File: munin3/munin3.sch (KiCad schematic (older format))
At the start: 79 parts, among them J1 Conn_Coaxial, J2 Conn_Coaxial, J3 Conn_01x02_Male, J4 Conn_01x02_Male, T1 Q_NMOS_DSG, T2 Q_NMOS_DSG, T3 BSS84, T4 BST82, U1 MC78L08_SO8, U2 LMC6482

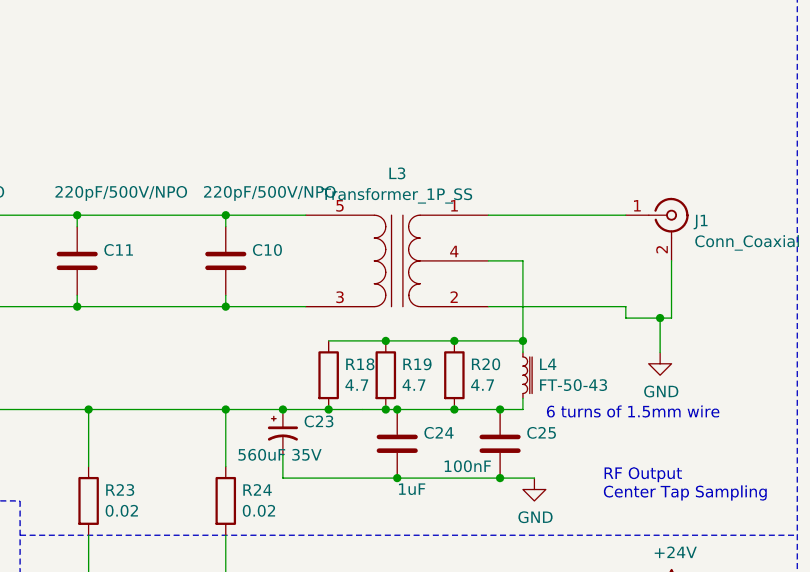
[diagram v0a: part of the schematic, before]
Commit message: Fixed drain connection, fixed final xfmr connection
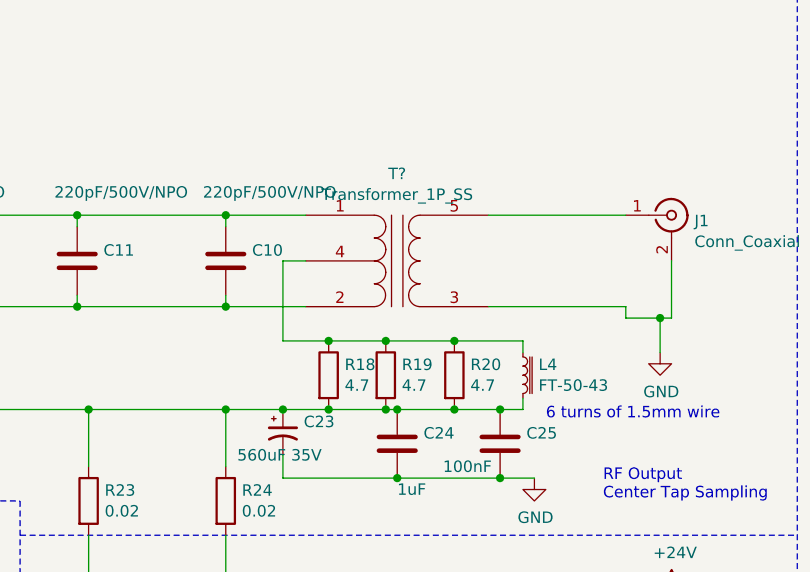
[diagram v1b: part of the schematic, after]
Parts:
- removed L3: Transformer_1P_SS, Transformer_THT:HF_Power_Xfmr, symbol Device:Transformer_1P_SS
- added T?: Transformer_1P_SS, symbol Device:Transformer_1P_SS
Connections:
- net GND: now also T?.3 (AB)
- net at C10.1, C11.1, C12.1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: now also T?.1 (SB)
- net at C10.2, C11.2, C12.2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: now also T?.2 (SA)
- net at J1.1 (In): now also T?.5 (AA)
- net at L4.1, R18.1, R19.1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: now also T?.4 (SC)
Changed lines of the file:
@@
 Wire Wire Line
 	7900 2150 8550 2150
-$Comp
-L Device:Transformer_1P_SS L3
-U 1 1 6165D7D3
-P 9300 1950
-F 0 "L3" H 9300 2331 50  0000 C CNN
-F 1 "Transformer_1P_SS" H 9300 2240 50  0000 C CNN
-F 2 "Transformer_THT:HF_Power_Xfmr" H 9300 1950 50  0001 C CNN
-F 3 "~" H 9300 1950 50  0001 C CNN
-	1    9300 1950
-	1    0    0    -1
-$EndComp
 Wire Wire Line
 	8550 1750 8900 1750
@@
 $EndComp
 Wire Wire Line
-	9700 1950 9850 1950
-Wire Wire Line
-	9850 1950 9850 2300
-Wire Wire Line
 	9550 2300 9850 2300
-Connection ~ 9850 2300
 Wire Wire Line
 	9850 2300 9850 2350
@@
 	9000 2300 9250 2300
 Connection ~ 9250 2300
-Wire Wire Line
-	9000 2600 9150 2600
 Wire Wire Line
 	9250 2600 9300 2600
@@
 Wire Wire Line
 	9750 2600 9850 2600
-Wire Wire Line
-	9150 2600 9250 2600
 $Comp
 L power:GND #PWR0108
@@
 Wire Wire Line
 	8800 2900 9300 2900
+Wire Wire Line
+	9000 2600 9250 2600
+$Comp
+L Device:Transformer_1P_SS T?
+U 1 1 61AC9DBF
+P 9300 1950
+F 0 "T?" H 9300 2331 50  0000 C CNN
+F 1 "Transformer_1P_SS" H 9300 2240 50  0000 C CNN
+F 2 "" H 9300 1950 50  0001 C CNN
+F 3 "~" H 9300 1950 50  0001 C CNN
+	1    9300 1950
+	-1   0    0    -1
+$EndComp
+Connection ~ 9000 2300
+Wire Wire Line
+	8900 1950 8800 1950
+Wire Wire Line
+	8800 1950 8800 2300
+Wire Wire Line
+	8800 2300 9000 2300
 $EndSCHEMATC

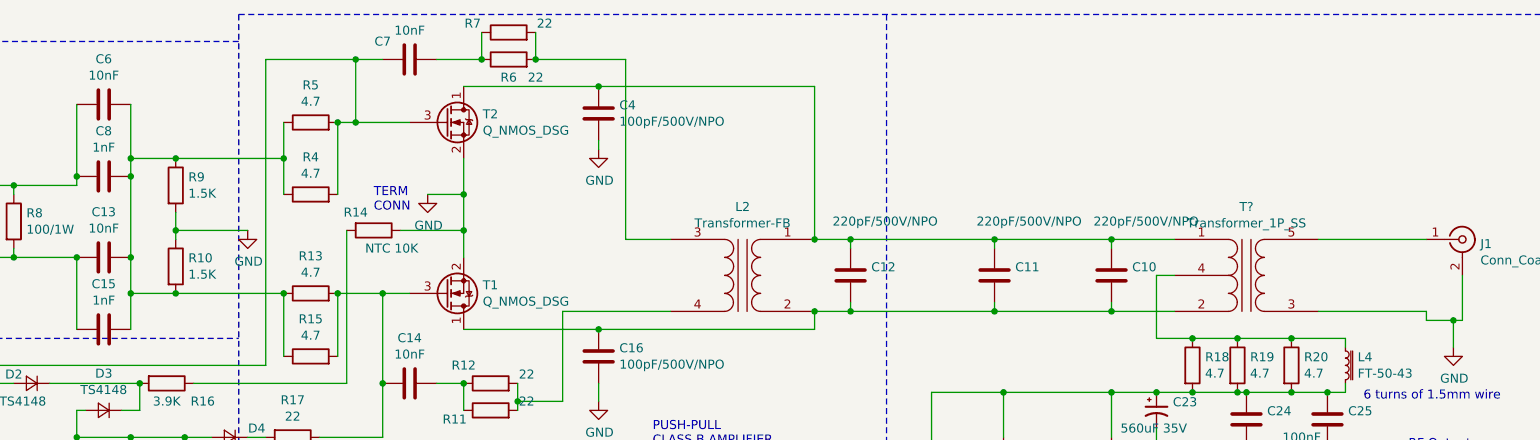
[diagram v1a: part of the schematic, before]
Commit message: Removed short between C8 and C15 on schem. Beefed up power/ground/Power Xfmr connections.
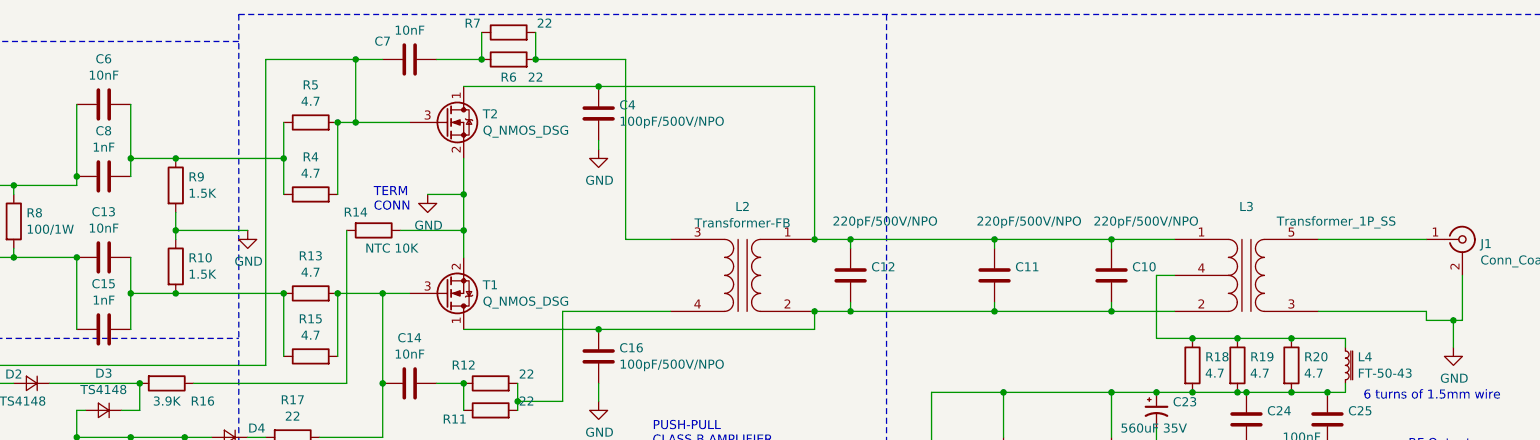
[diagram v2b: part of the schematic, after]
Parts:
- L3: renamed from T?; footprint (none) -> Transformer_THT:HF_Power_Xfmr
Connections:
- net at C6.1, C8.1, R4.1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: no longer C13.1, C15.1, R10.2, R13.1, R15.1
- new net: C13.1, C15.1, R10.2, R13.1, R15.1
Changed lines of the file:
@@
 Wire Wire Line
 	3100 1000 3100 1300
-Connection ~ 3100 1850
 Wire Wire Line
 	3100 1850 3100 2050
-Connection ~ 3100 1400
-Wire Wire Line
-	3100 1400 3100 1850
 Wire Wire Line
 	3350 1300 3100 1300
@@
 	9000 2600 9250 2600
 $Comp
-L Device:Transformer_1P_SS T?
+L Device:Transformer_1P_SS L3
 U 1 1 61AC9DBF
 P 9300 1950
-F 0 "T?" H 9300 2331 50  0000 C CNN
-F 1 "Transformer_1P_SS" H 9300 2240 50  0000 C CNN
-F 2 "" H 9300 1950 50  0001 C CNN
+F 0 "L3" H 9300 2331 50  0000 C CNN
+F 1 "Transformer_1P_SS" H 8800 2250 50  0000 C CNN
+F 2 "Transformer_THT:HF_Power_Xfmr" H 9300 1950 50  0001 C CNN
 F 3 "~" H 9300 1950 50  0001 C CNN
 	1    9300 1950
